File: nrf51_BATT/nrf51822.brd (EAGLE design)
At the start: 38.2 x 26.4 mm, 20 parts, among them T1 MMUN2238

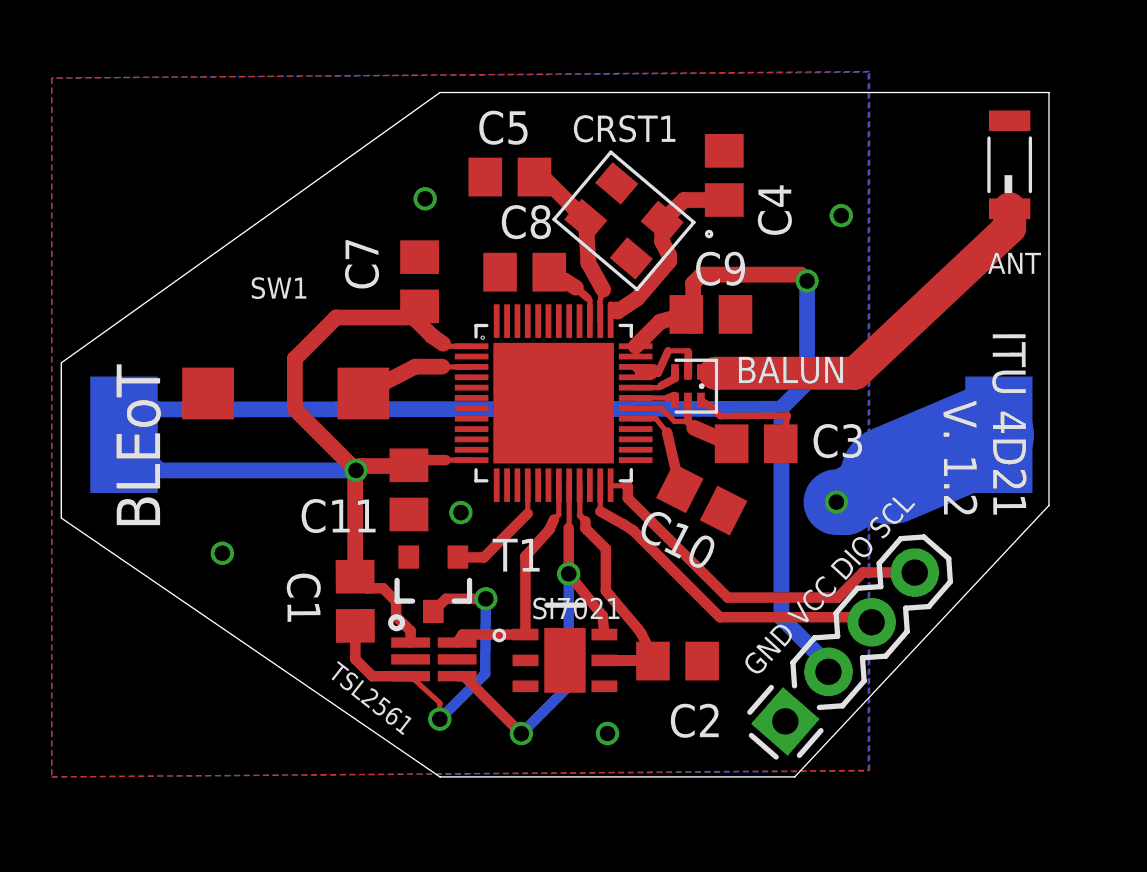
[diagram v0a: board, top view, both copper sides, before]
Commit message: Cleaned sensor board v.1.2 - TAG AS SENT TO SMART PROTOTYPE Cleaned actuation board v.1.0 - TAG AS SENT TO SMART PROTOTYPE Made a compact version of the sensor board - TAG AS SENT TO SMART PROTOTYPE
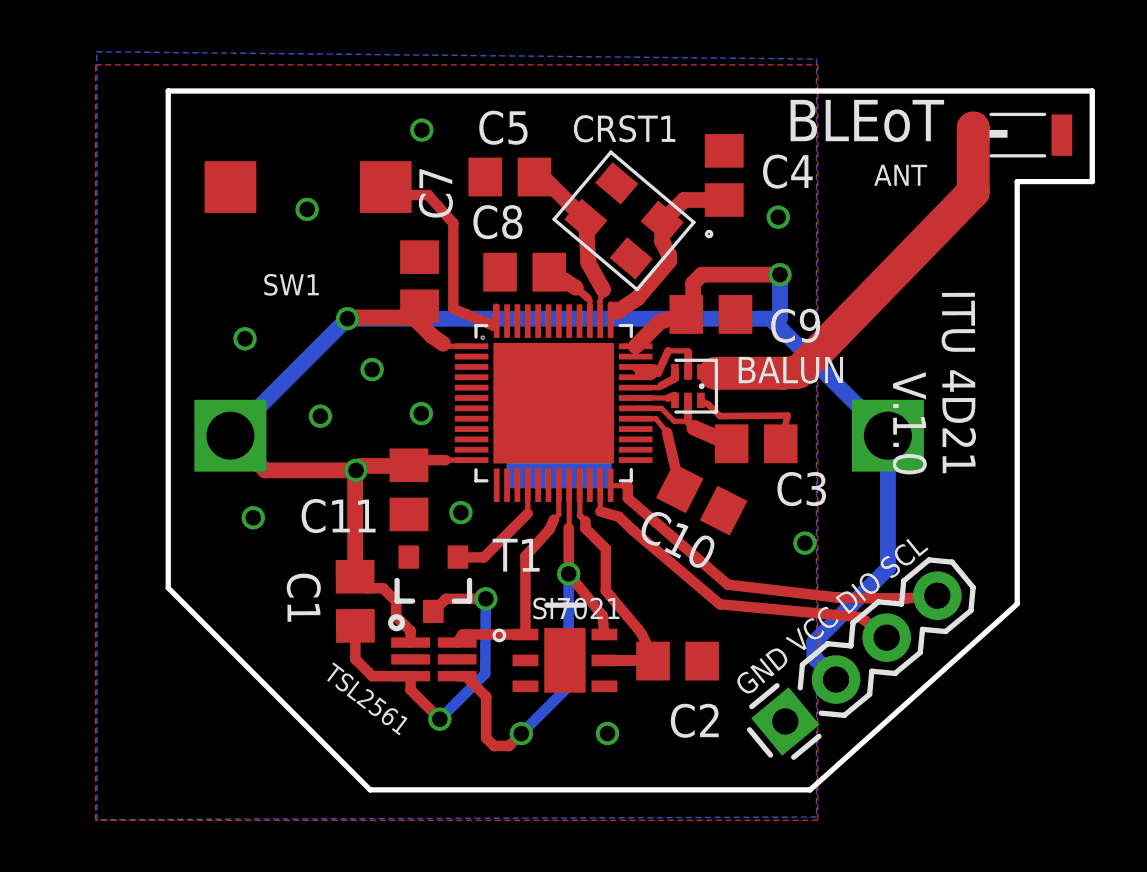
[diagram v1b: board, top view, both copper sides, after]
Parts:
- removed CR2450: 3.3V, NordicSemi:CR2450
- added BAT1: (no value), SparkFun-Electromechanical:BATTCON_245MM_PTH
- moved SW1 8.02 mm to (9.60, 22.8)
- moved ANT 1.19 mm to (37.0, 24.8), turned to 0 degrees
- turned JP1 to 39.6 degrees
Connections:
- new net GPIO9: SW1.P$2, U$4.48
- net GIOP8: no longer SW1.P$2
- net GND: now also BAT1.2; no longer CR2450.NEG
- net VDD: now also BAT1.1, BAT1.3; no longer CR2450.POS
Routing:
- net VDD: track 90.4 -> 75.1 mm, vias 2 -> 3
- net GPIO9: track 0.00 -> 10.2 mm
- net GND: track 17.0 -> 10.3 mm, vias 6 -> 11
- net GIOP8: track 5.07 -> 0.00 mm
- net GIOP6: track 16.6 -> 17.9 mm
- net N$3: track 15.1 -> 16.4 mm
- net N$8: track 13.1 -> 13.7 mm
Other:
- board size 38.2 x 26.4 mm -> 35.7 x 27 mm
- board text added: "ITU 4D21 V.1.0"
- board text removed: "ITU 4D21 V. 1.2"

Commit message: Sent to smart-prototype Actuation 1.2 Compact 1.1
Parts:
- moved ANT 2.90 mm to (34.1, 24.9)
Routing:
- net N$3: track 16.4 -> 15.3 mm
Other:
- board size 35.7 x 27 mm -> 32.8 x 27 mm
- board text removed: "BLEoT"
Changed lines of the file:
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@@
 <board>
 <plain>
-<text x="34.169" y="26.159" size="1.6" layer="21" rot="R180">BLEoT</text>
 <text x="35.3906" y="11.5918" size="1.27" layer="21" rot="R90.2">ITU 4D21
 V.1.0</text>
@@
 <wire x1="12" y1="-0.5" x2="29" y2="-0.5" width="0.2032" layer="20"/>
 <wire x1="29" y1="-0.5" x2="37" y2="6.6802" width="0.2032" layer="20"/>
-<wire x1="39.9" y1="26.5" x2="4.2" y2="26.5" width="0.2032" layer="20"/>
+<wire x1="37" y1="26.5" x2="4.2" y2="26.5" width="0.2032" layer="20"/>
 <wire x1="4.2" y1="26.5" x2="4.2" y2="7.3" width="0.2032" layer="20"/>
 <wire x1="4.2" y1="7.3" x2="12" y2="-0.5" width="0.2032" layer="20"/>
-<wire x1="39.9" y1="26.5" x2="39.9" y2="23" width="0.2032" layer="20"/>
-<wire x1="39.9" y1="23" x2="37" y2="23" width="0.2032" layer="20"/>
-<wire x1="37" y1="23" x2="37" y2="6.7" width="0.2032" layer="20"/>
+<wire x1="37" y1="26.5" x2="37" y2="6.7" width="0.2032" layer="20"/>
 </plain>
 <attributes>
@@
 <attribute name="NAME" x="23.9082375" y="25.549421875" size="1.016" layer="21" rot="R180"/>
 </element>
-<element name="ANT" library="NordicSemi" package="2450AT18B100" value="ANTENA-2450AT" x="37.0254" y="24.7956" smashed="yes">
-<attribute name="NAME" x="33.5174" y="23.6508" size="0.8128" layer="25" rot="R180"/>
+<element name="ANT" library="NordicSemi" package="2450AT18B100" value="ANTENA-2450AT" x="34.1254" y="24.8956" smashed="yes">
+<attribute name="NAME" x="36.2174" y="22.7508" size="0.8128" layer="25" rot="R180"/>
 </element>
 <element name="U$4" library="NordicSemi" package="QFN48" value="NRF51822" x="19.09" y="14.44" smashed="yes"/>
@@
 <wire x1="26.035" y1="17.78" x2="26.116" y2="17.8672" width="0.2032" layer="1"/>
 <wire x1="26.035" y1="17.78" x2="25.99419375" y2="17.745378125" width="0.2032" layer="1"/>
-<via x="28.7972" y="9.0332" extent="1-16" drill="0.6"/>
+<via x="27.7972" y="9.0332" extent="1-16" drill="0.6"/>
 <via x="10.078" y="13.9368" extent="1-16" drill="0.6"/>
 <via x="27.7664" y="21.626" extent="1-16" drill="0.6"/>
@@
 <wire x1="25.3746" y1="15.5956" x2="24.7806" y2="15.5194" width="0.3048" layer="1"/>
 <wire x1="24.7806" y1="15.5194" x2="24.78" y2="15.647" width="0.3048" layer="1"/>
-<wire x1="27.934" y1="15.5956" x2="28.534" y2="15.634" width="1.27" layer="1"/>
-<wire x1="28.534" y1="15.634" x2="35.3" y2="22.6" width="1.27" layer="1"/>
-<wire x1="35.3" y1="22.6" x2="35.3" y2="25.0702" width="1.27" layer="1"/>
-<wire x1="35.3" y1="25.0702" x2="35.3254" y2="24.7956" width="1.27" layer="1"/>
+<wire x1="27.934" y1="15.5956" x2="28.554" y2="15.584" width="1.27" layer="1"/>
+<wire x1="28.554" y1="15.584" x2="28.754" y2="15.584" width="1.27" layer="1"/>
+<wire x1="28.754" y1="15.584" x2="32.6" y2="19.5" width="1.27" layer="1"/>
+<wire x1="32.6" y1="19.5" x2="32.6" y2="25.1702" width="1.27" layer="1"/>
+<wire x1="32.6" y1="25.1702" x2="32.4254" y2="24.8956" width="0" layer="19" extent="1-1"/>
 </signal>
 <signal name="N$4">
@@
 <wire x1="22.26" y1="14.24" x2="23.2504" y2="14.24" width="0.2032" layer="1"/>
 <wire x1="23.2504" y1="14.24" x2="23.749" y2="13.7414" width="0.2032" layer="1"/>
-<wire x1="23.749" y1="13.7414" x2="24.2656" y2="13.7414" width="0.2032" layer="1"/>
+<wire x1="23.749" y1="13.7414" x2="24.2656" y2="13.7414" width="0.254" layer="1"/>
 <wire x1="24.2656" y1="13.7414" x2="24.28" y2="13.727" width="0.2032" layer="1"/>
 </signal>
